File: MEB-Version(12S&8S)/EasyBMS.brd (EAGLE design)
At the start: 48.9 x 100 mm, 174 parts, among them IC1 XL7046, IC2 LTC6811IG-1#PBF, IC3 ISO1042DWV, IC4 AMS1117-3.3, J1 TYPE-C-31-M-12, Q14 C8547, Q15 C8547, Q16 C8547, Q18 C8547, Q20 C8547, Q22 C8547, Q24 C8547, Q26 C8547, Q28 C8547, Q30 C8547, Q32 C8547, Q34 C8547, U1 ESP32-C6-MINI-1-N4, Y1 FC-135_32.7680KA-A5

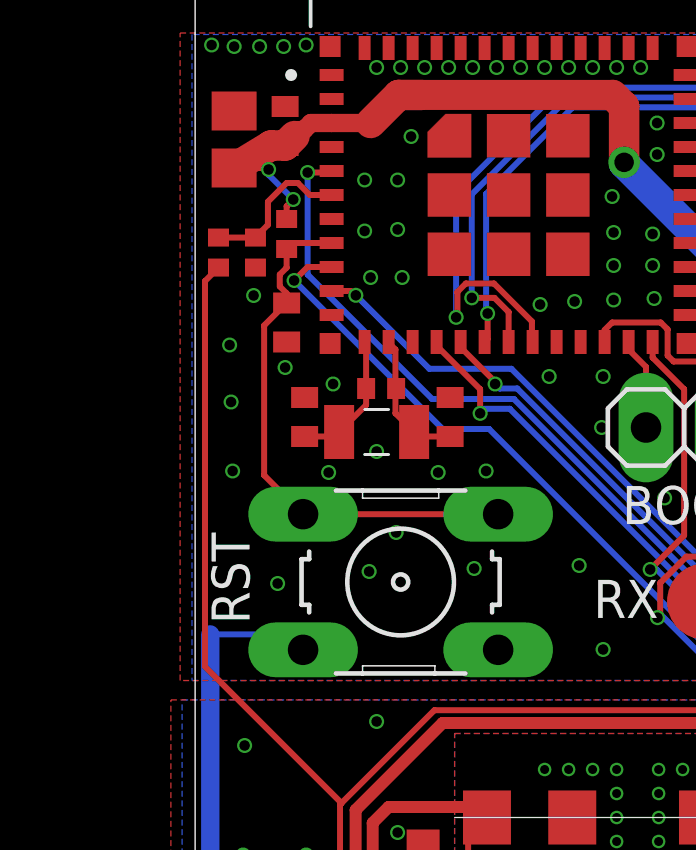
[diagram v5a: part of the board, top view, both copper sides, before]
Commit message: new Footprint to change to basic parts
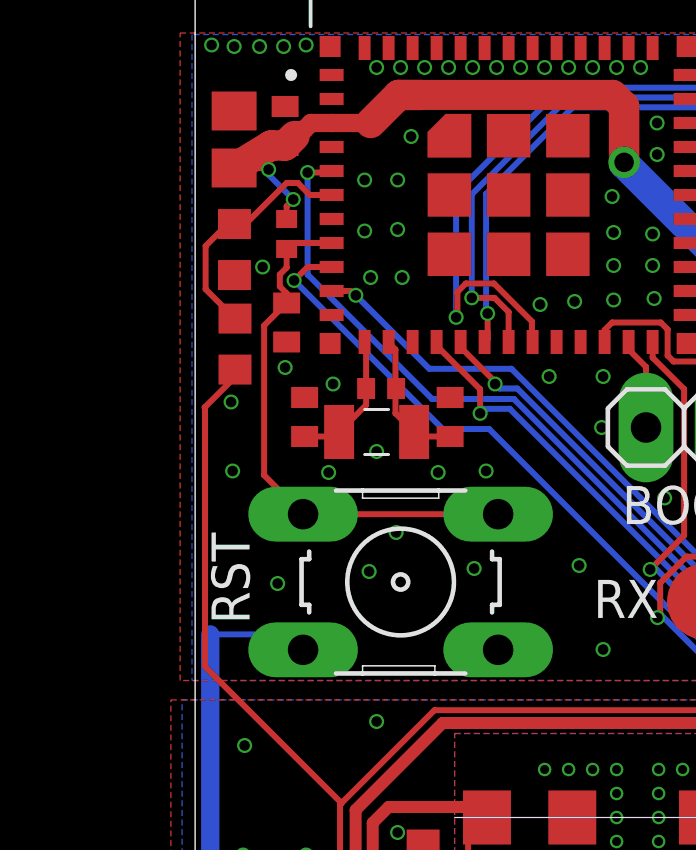
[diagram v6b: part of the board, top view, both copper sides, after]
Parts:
- C12, C14: value 47µF -> 47uF
- R15, R16: device rcl:R0402 -> rcl:R0603
- moved R15 3.10 mm to (1.48, 83.7)
- moved R16 0.71 mm to (1.46, 86.8)
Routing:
- net MODULEVOLTAGE: track 5.15 -> 8.58 mm
- net C12+POWER: track 67.8 -> 64.6 mm
- net GND: vias 121 -> 120
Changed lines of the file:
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@@
 <drawing>
 <settings>
-<setting alwaysvectorfont="yes"/>
+<setting alwaysvectorfont="no"/>
 <setting verticaltext="up"/>
 </settings>
@@
 </groups>
 <elements>
-<element name="R15" library="rcl" library_urn="urn:adsk.eagle:library:334" package="R0402" package3d_urn="urn:adsk.eagle:package:23547/3" value="470k" x="0.9292" y="86.7308" smashed="yes" rot="R270">
-<attribute name="POPULARITY" value="0" x="0.9292" y="86.7308" size="1.778" layer="27" rot="R270" display="off"/>
-<attribute name="SPICEPREFIX" value="R" x="0.9292" y="86.7308" size="1.778" layer="27" rot="R270" display="off"/>
-</element>
-<element name="R16" library="rcl" library_urn="urn:adsk.eagle:library:334" package="R0402" package3d_urn="urn:adsk.eagle:package:23547/3" value="27K" x="2.1612" y="86.7308" smashed="yes" rot="R90">
-<attribute name="POPULARITY" value="0" x="2.1612" y="86.7308" size="1.778" layer="27" rot="R90" display="off"/>
-<attribute name="SPICEPREFIX" value="R" x="2.1612" y="86.7308" size="1.778" layer="27" rot="R90" display="off"/>
+<element name="R15" library="rcl" library_urn="urn:adsk.eagle:library:334" package="R0603" package3d_urn="urn:adsk.eagle:package:23555/3" value="470k" x="1.4792" y="83.6808" smashed="yes" rot="R270">
+<attribute name="POPULARITY" value="70" x="1.4792" y="83.6808" size="1.778" layer="27" rot="R270" display="off"/>
+<attribute name="SPICEPREFIX" value="R" x="1.4792" y="83.6808" size="1.778" layer="27" rot="R270" display="off"/>
+</element>
+<element name="R16" library="rcl" library_urn="urn:adsk.eagle:library:334" package="R0603" package3d_urn="urn:adsk.eagle:package:23555/3" value="27K" x="1.4612" y="86.8308" smashed="yes" rot="R90">
+<attribute name="POPULARITY" value="70" x="1.4612" y="86.8308" size="1.778" layer="27" rot="R90" display="off"/>
+<attribute name="SPICEPREFIX" value="R" x="1.4612" y="86.8308" size="1.778" layer="27" rot="R90" display="off"/>
 </element>
 <element name="C4" library="rcl" library_urn="urn:adsk.eagle:library:334" package="C0402" package3d_urn="urn:adsk.eagle:package:23626/2" value="1uF" x="44.45" y="33.75" smashed="yes">
@@
 <attribute name="VALUE" x="45.9499" y="9.75" size="0.02" layer="27" rot="R180"/>
 </element>
-<element name="C12" library="rcl" library_urn="urn:adsk.eagle:library:334" package="C1206" package3d_urn="urn:adsk.eagle:package:23618/2" value="47µF" x="42.35" y="10.9" smashed="yes" rot="R90">
+<element name="C12" library="rcl" library_urn="urn:adsk.eagle:library:334" package="C1206" package3d_urn="urn:adsk.eagle:package:23618/2" value="47uF" x="42.35" y="10.9" smashed="yes" rot="R90">
 <attribute name="POPULARITY" value="54" x="42.35" y="10.9" size="1.778" layer="27" rot="R90" display="off"/>
 <attribute name="SPICEPREFIX" value="C" x="42.35" y="10.9" size="1.778" layer="27" rot="R90" display="off"/>
@@
 <attribute name="VALUE" x="1.295" y="85.035" size="1.27" layer="27" rot="R270"/>
 </element>
-<element name="C14" library="rcl" library_urn="urn:adsk.eagle:library:334" package="C0805" package3d_urn="urn:adsk.eagle:package:23617/2" value="47µF" x="1.45" y="90.5" smashed="yes" rot="R90">
+<element name="C14" library="rcl" library_urn="urn:adsk.eagle:library:334" package="C0805" package3d_urn="urn:adsk.eagle:package:23617/2" value="47uF" x="1.45" y="90.5" smashed="yes" rot="R90">
 <attribute name="POPULARITY" value="88" x="1.45" y="90.5" size="1.778" layer="27" rot="R90" display="off"/>
 <attribute name="SPICEPREFIX" value="C" x="1.45" y="90.5" size="1.778" layer="27" rot="R90" display="off"/>
@@
 <via x="11.95" y="82.6" extent="1-16" drill="0.35"/>
 <via x="20.55" y="87.75" extent="1-16" drill="0.35"/>
-<via x="2.1" y="85.3" extent="1-16" drill="0.35"/>
 <via x="0.7" y="93.65" extent="1-16" drill="0.35"/>
 <via x="11.8" y="92.9" extent="1-16" drill="0.35"/>
@@
 <via x="14.1" y="85.15" extent="1-16" drill="0.35"/>
 <via x="6.2" y="92.9" extent="1-16" drill="0.35"/>
-<via x="1.3" y="83.65" extent="1-16" drill="0.35"/>
 <via x="4.75" y="82.35" extent="1-16" drill="0.35"/>
 <via x="6.85" y="77.4" extent="1-16" drill="0.35"/>
@@
 <via x="22.05" y="96.15" extent="1-16" drill="0.35"/>
 <via x="25.2" y="90.9" extent="1-16" drill="0.35"/>
+<via x="2.4" y="86.25" extent="1-16" drill="0.35"/>
 </signal>
 <signal name="N$202">
@@
 <contactref element="R15" pad="1"/>
 <contactref element="R16" pad="2"/>
-<wire x1="0.9292" y1="87.2308" x2="2.1612" y2="87.2308" width="0.2" layer="1"/>
 <contactref element="U1" pad="6"/>
-<wire x1="2.577" y1="87.655975" x2="2.577" y2="88.427" width="0.2" layer="1"/>
-<wire x1="2.577" y1="88.427" x2="3.2" y2="89.05" width="0.2" layer="1"/>
-<wire x1="2.1612" y1="87.2308" x2="2.1612" y2="87.240175" width="0.2" layer="1"/>
-<wire x1="2.1612" y1="87.240175" x2="2.577" y2="87.655975" width="0.2" layer="1"/>
+<wire x1="1.4612" y1="87.6808" x2="1.4612" y2="87.3112" width="0.2" layer="1"/>
+<wire x1="1.4612" y1="87.3112" x2="3.2" y2="89.05" width="0.2" layer="1"/>
 <wire x1="3.2" y1="89.05" x2="3.57371875" y2="89.05" width="0.2" layer="1"/>
 <wire x1="3.57371875" y1="89.05" x2="3.97371875" y2="88.65" width="0.2" layer="1"/>
 <wire x1="3.97371875" y1="88.65" x2="4.7" y2="88.65" width="0.2" layer="1"/>
+<wire x1="1.4792" y1="84.5308" x2="0.5" y2="85.51" width="0.2" layer="1"/>
+<wire x1="0.5" y1="85.51" x2="0.5" y2="86.95" width="0.2" layer="1"/>
+<wire x1="0.5" y1="86.95" x2="1.2308" y2="87.6808" width="0.2" layer="1"/>
+<wire x1="1.2308" y1="87.6808" x2="1.4612" y2="87.6808" width="0.2" layer="1"/>
 </signal>
 <signal name="VREF2">
@@
 <wire x1="24.3964" y1="72.905" x2="22.9684" y2="71.477" width="0.2" layer="1"/>
 <wire x1="5.03" y1="68.38" x2="0.4792" y2="72.9308" width="0.2" layer="1"/>
-<wire x1="0.9292" y1="86.2308" x2="0.4792" y2="85.7808" width="0.2" layer="1"/>
-<wire x1="0.4792" y1="85.7808" x2="0.4792" y2="72.9308" width="0.2" layer="1"/>
+<wire x1="1.4792" y1="82.8308" x2="1.4792" y2="82.5808" width="0.2" layer="1"/>
+<wire x1="1.4792" y1="82.5808" x2="0.46606875" y2="81.56766875" width="0.2" layer="1"/>
+<wire x1="0.4792" y1="81.508578125" x2="0.46606875" y2="81.56766875" width="0.2" layer="1"/>
+<wire x1="0.4792" y1="81.508578125" x2="0.4792" y2="72.9308" width="0.2" layer="1"/>
 </signal>
 <signal name="GND2">
